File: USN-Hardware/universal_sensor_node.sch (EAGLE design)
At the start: 20 parts, among them J2 SSQ-110-03-T-S, J3 JST_S2B-ZR-SM4A-TF_LF_SNJST_S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, J4 10118192-0001LF, J5 SSQ-110-03-T-S, U1 MCP73831T-2ACI/OT, U2 ATMEGA328PB-AU, Y1 TSX-3225EPSON_TSX-3225_16.000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

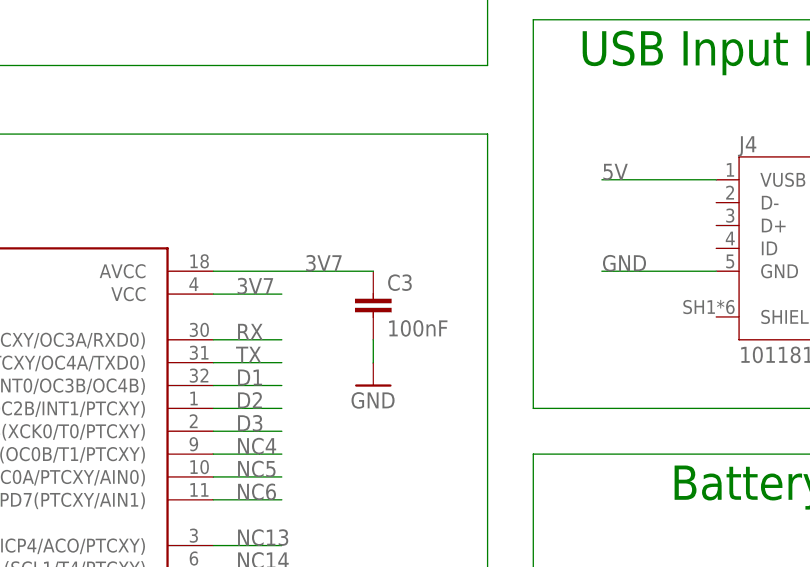
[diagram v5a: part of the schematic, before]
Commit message: updated parts attributes for bom.
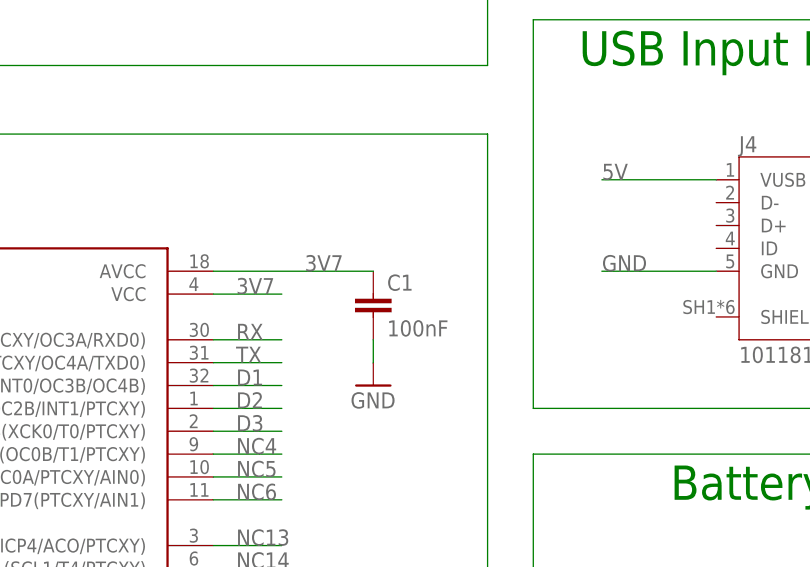
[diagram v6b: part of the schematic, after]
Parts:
- removed C3: 100nF, universal_sensor_node:100NF-50V-5%(0603)
- added C1: 100nF, universal_sensor_node:100NF-50V-10%(0603)
- U2: device ATMEGA328PB-AU:ATMEGA328PB-AU -> universal_sensor_node:ATMEGA328PB-AU
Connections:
- net 3V7: now also C1.1; no longer C3.1
- net GND: now also C1.2; no longer C3.2
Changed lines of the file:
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@@
 <part name="GND8" library="supply1" deviceset="GND" device=""/>
 <part name="LOGO1" library="SparkFun-Aesthetics" deviceset="OSHW-LOGO" device="MINI"/>
-<part name="U2" library="ATMEGA328PB-AU" deviceset="ATMEGA328PB-AU" device=""/>
-<part name="C3" library="universal_sensor_node" deviceset="100NF-50V-5%(0603)" device="" value="100nF"/>
+<part name="U2" library="universal_sensor_node" deviceset="ATMEGA328PB-AU" device=""/>
 <part name="Y1" library="universal_sensor_node" deviceset="TSX-3225" device="EPSON_TSX-3225_16.0000MF09Z-AC3_0_0"/>
 <part name="C4" library="universal_sensor_node" deviceset="9PF-50V(0603)" device="" value="9pF"/>
@@
 <part name="U1" library="universal_sensor_node" deviceset="MCP73831T-2ACI/OT" device=""/>
 <part name="GND1" library="supply1" deviceset="GND" device=""/>
+<part name="C1" library="universal_sensor_node" deviceset="100NF-50V-10%(0603)" device="" value="100nF"/>
 </parts>
 <sheets>
@@
 <attribute name="VALUE" x="4.9472" y="18.8527" size="2.5558" layer="96"/>
 </instance>
-<instance part="C3" gate="G$1" x="104.14" y="71.12" smashed="yes">
-<attribute name="NAME" x="105.664" y="74.041" size="1.778" layer="95"/>
-<attribute name="VALUE" x="105.664" y="68.961" size="1.778" layer="96"/>
-</instance>
 <instance part="Y1" gate="G$0" x="-35.56" y="55.88" smashed="yes">
 <attribute name="NAME" x="-32.766" y="56.388" size="2.54" layer="95" align="top-left"/>
@@
 <instance part="GND1" gate="1" x="-25.4" y="40.64" smashed="yes">
 <attribute name="VALUE" x="-27.94" y="38.1" size="1.778" layer="96"/>
+</instance>
+<instance part="C1" gate="G$1" x="104.14" y="71.12" smashed="yes">
+<attribute name="NAME" x="105.664" y="74.041" size="1.778" layer="95"/>
+<attribute name="VALUE" x="105.664" y="68.961" size="1.778" layer="96"/>
 </instance>
 </instances>
@@
 <wire x1="86.36" y1="76.2" x2="104.14" y2="76.2" width="0.1524" layer="91"/>
 <label x="96.52" y="76.2" size="1.778" layer="95"/>
-<pinref part="C3" gate="G$1" pin="1"/>
+<pinref part="C1" gate="G$1" pin="1"/>
 </segment>
 <segment>
@@
 <pinref part="GND7" gate="1" pin="GND"/>
 <wire x1="104.14" y1="68.58" x2="104.14" y2="66.04" width="0.1524" layer="91"/>
-<pinref part="C3" gate="G$1" pin="2"/>
-</segment>
-<segment>
+<pinref part="C1" gate="G$1" pin="2"/>
+</segment>
+<segment>
